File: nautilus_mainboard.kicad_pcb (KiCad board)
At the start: 4 copper layers, 176.2 x 77.5 mm, 52 parts, among them J18 179-UJ20CHC4SMTTR, J3 1761681-3, J4 Header male 1x05, J7 LPHT-04-16-L-RT1-GP, SW1 Button Switch SPST-No

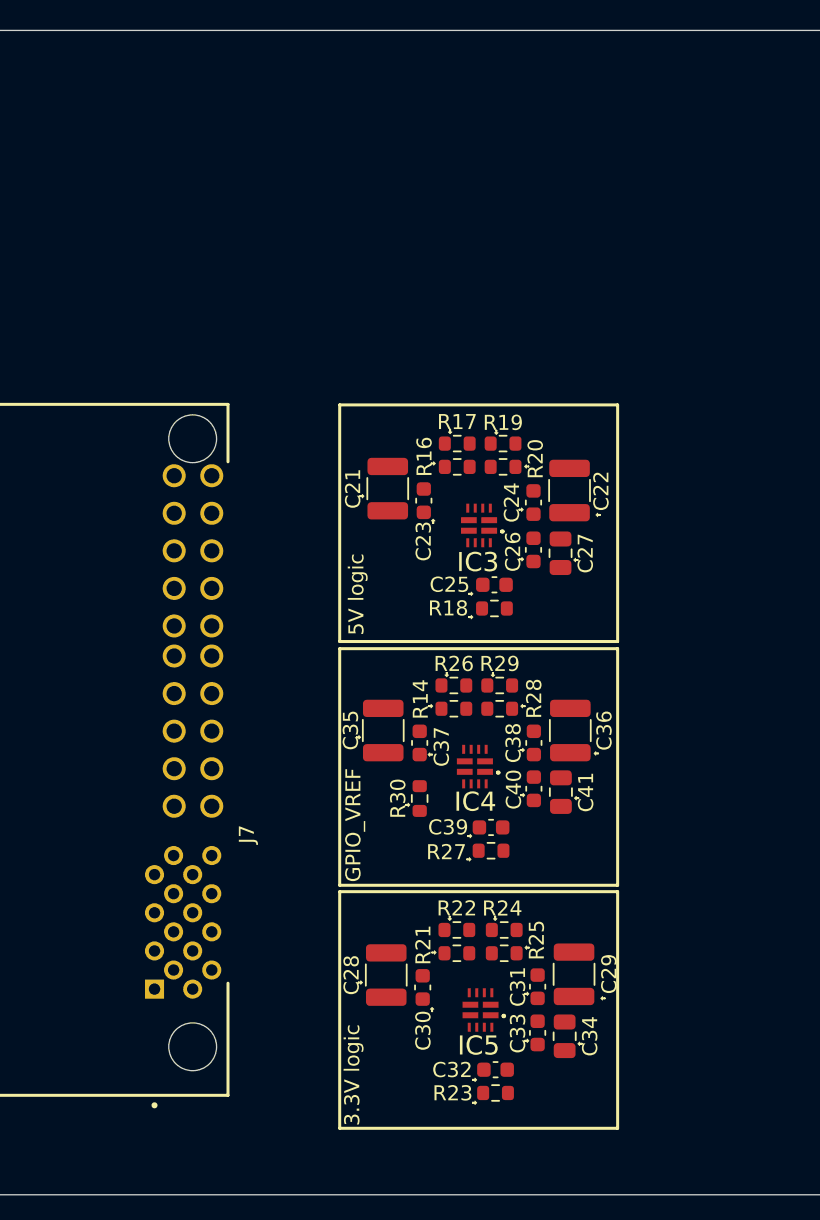
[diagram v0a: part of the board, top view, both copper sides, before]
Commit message: multiple changes to the differential pair for easier routing later.
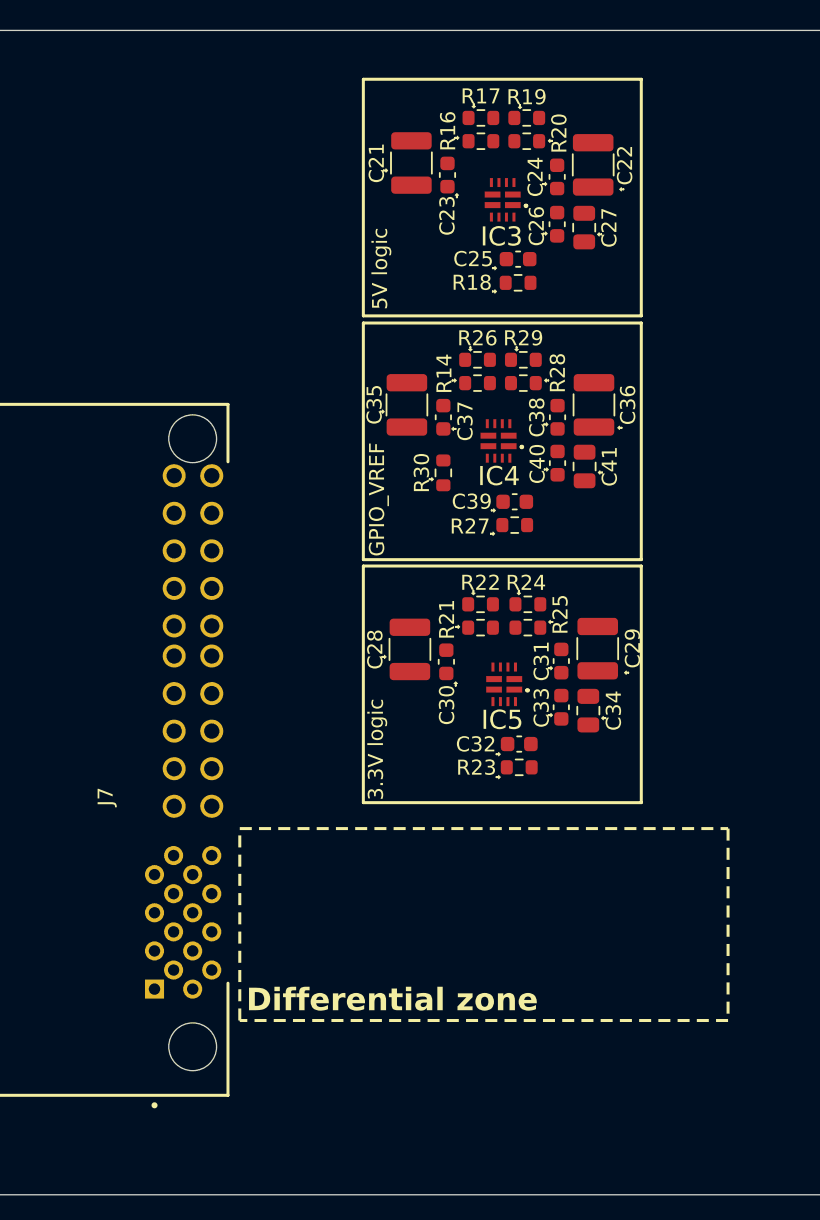
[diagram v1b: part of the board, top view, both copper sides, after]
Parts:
- moved C31 21.7 mm to (108.8, 89.5)
- moved R14 21.7 mm to (103.2, 71.0)
- moved R28 21.7 mm to (106.3, 71.0)
- moved C25 21.7 mm to (106.0, 62.7)
- moved C26 21.7 mm to (108.5, 60.4)
- moved IC3 21.7 mm to (104.9, 58.8)
- moved C21 21.7 mm to (98.8, 56.3)
- moved C22 21.7 mm to (111.0, 56.5)
- moved C23 21.7 mm to (101.2, 57.1)
- moved C24 21.7 mm to (108.5, 57.2)
- moved C27 21.7 mm to (110.3, 60.6)
- moved C28 21.7 mm to (98.8, 88.7)
- moved C29 21.7 mm to (111.2, 88.7)
- moved C30 21.7 mm to (101.2, 89.5)
- moved C32 21.7 mm to (106.0, 95.0)
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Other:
- board text added: "Differential zone"

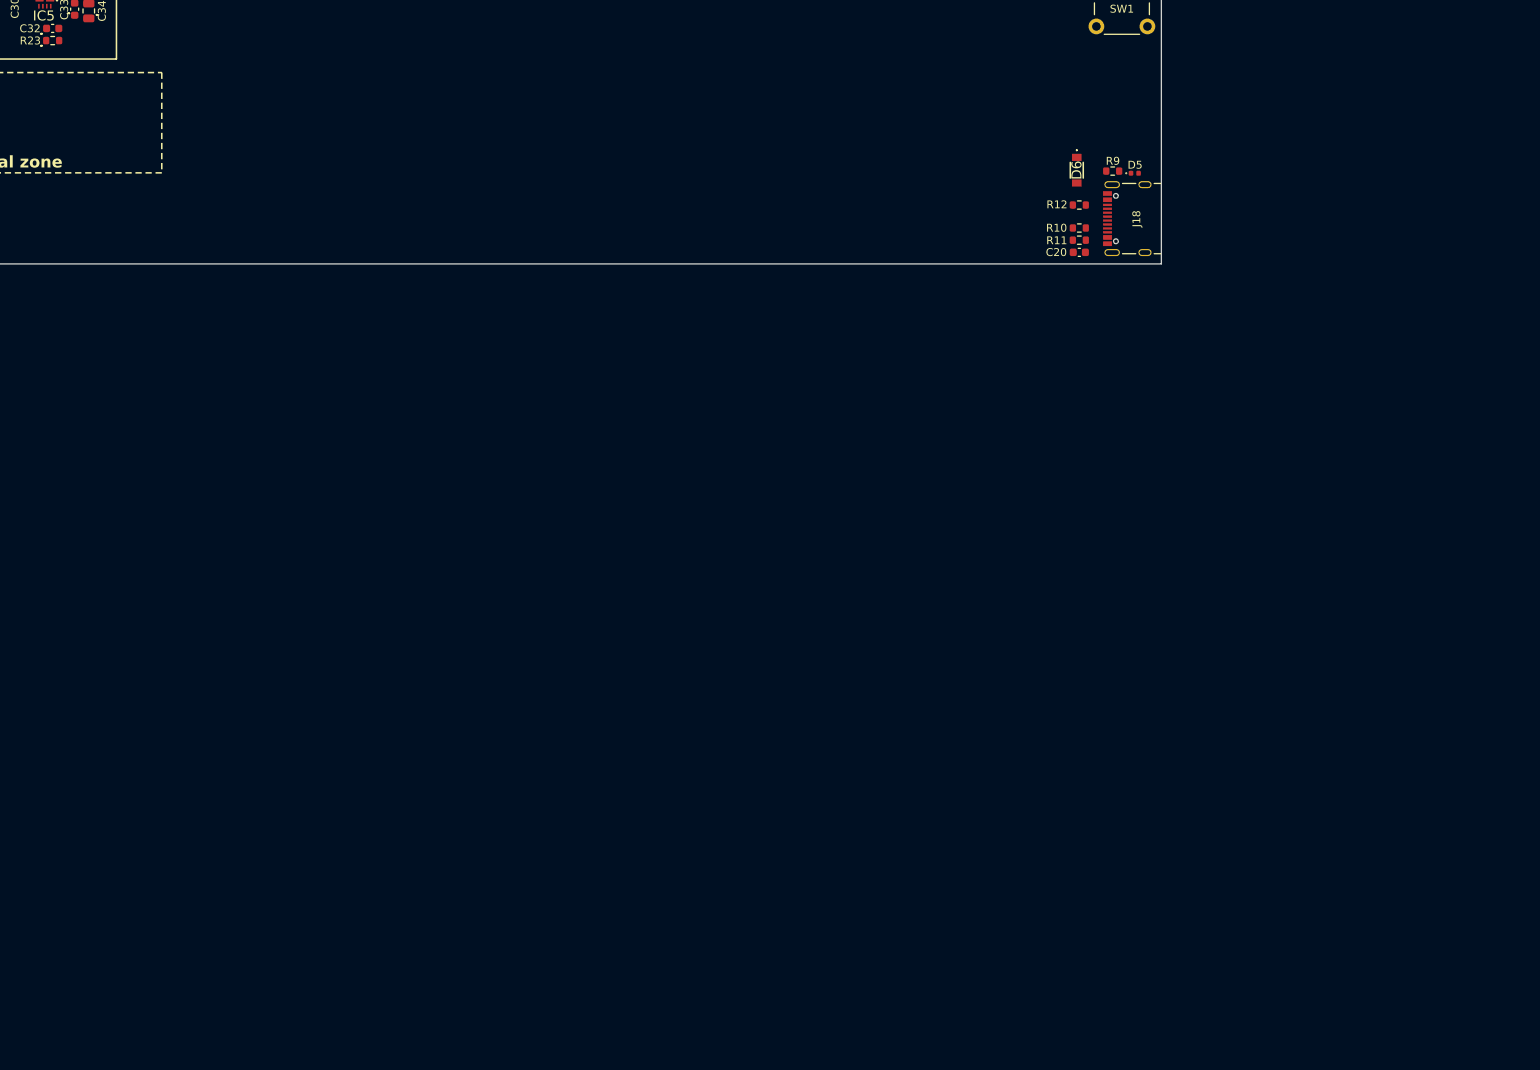
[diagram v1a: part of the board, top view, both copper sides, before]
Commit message: added Gyroscope and Accelerometer part (4x) over IIC
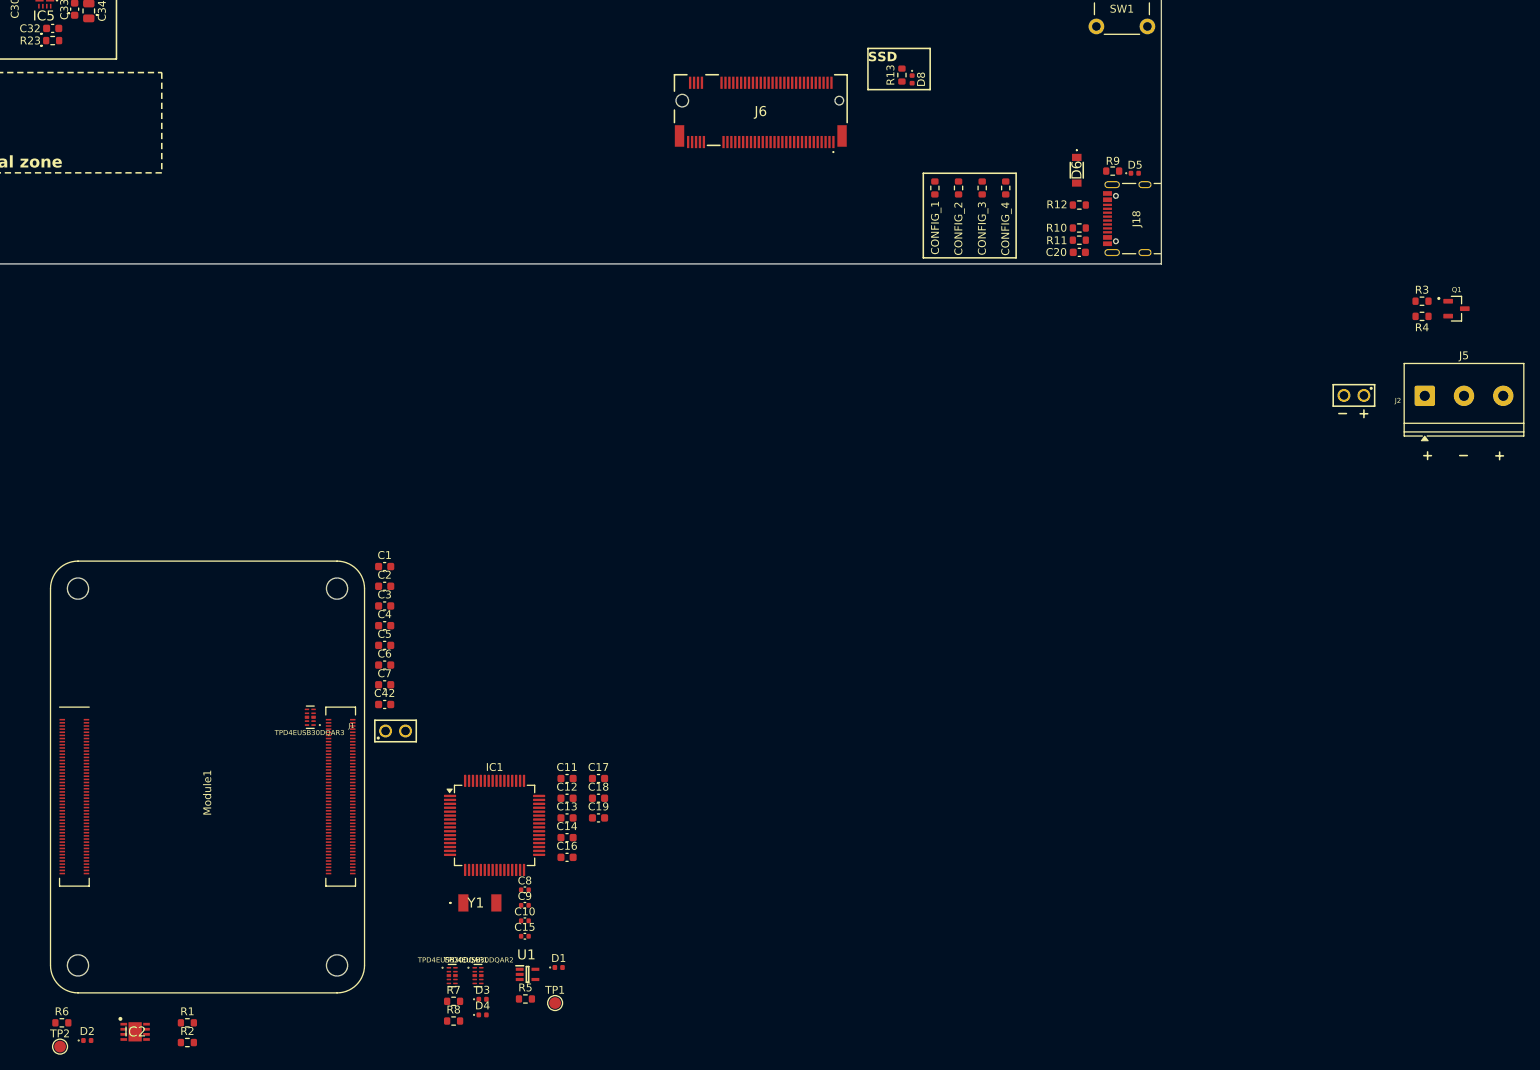
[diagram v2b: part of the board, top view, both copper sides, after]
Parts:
- added C1: 100nF, Capacitor_SMD:C_0603_1608Metric, F.Cu at (148.3, 163.6)
- added C10: 2.2pF, Capacitor_SMD:C_0402_1005Metric, F.Cu at (166.2, 208.7)
- added C11: 100nF, Capacitor_SMD:C_0603_1608Metric, F.Cu at (171.5, 190.6)
- added C12: 10pF, Capacitor_SMD:C_0603_1608Metric, F.Cu at (171.5, 193.1)
- added C13: 10pF, Capacitor_SMD:C_0603_1608Metric, F.Cu at (171.5, 195.6)
- added C14: 10pF, Capacitor_SMD:C_0603_1608Metric, F.Cu at (171.5, 198.1)
- added C15: 2.2pF, Capacitor_SMD:C_0402_1005Metric, F.Cu at (166.2, 210.6)
- added C16: 10pF, Capacitor_SMD:C_0603_1608Metric, F.Cu at (171.5, 200.6)
- added C17: 10pF, Capacitor_SMD:C_0603_1608Metric, F.Cu at (175.6, 190.6)
- added C18: 10pF, Capacitor_SMD:C_0603_1608Metric, F.Cu at (175.6, 193.1)
- added C19: 100nF, Capacitor_SMD:C_0603_1608Metric, F.Cu at (175.6, 195.6)
- added C2: 100nF, Capacitor_SMD:C_0603_1608Metric, F.Cu at (148.3, 166.1)
- added C3: 100nF, Capacitor_SMD:C_0603_1608Metric, F.Cu at (148.3, 168.6)
- added C4: 100nF, Capacitor_SMD:C_0603_1608Metric, F.Cu at (148.3, 171.1)
- added C42: 1uF, Capacitor_SMD:C_0603_1608Metric, F.Cu at (148.3, 181.1)
- added C5: 100nF, Capacitor_SMD:C_0603_1608Metric, F.Cu at (148.3, 173.6)
- added C6: 100nF, Capacitor_SMD:C_0603_1608Metric, F.Cu at (148.3, 176.1)
- added C7: 1uF, Capacitor_SMD:C_0603_1608Metric, F.Cu at (148.3, 178.6)
- added C8: 4.7pF, Capacitor_SMD:C_0402_1005Metric, F.Cu at (166.2, 204.7)
- added C9: 4.7pF, Capacitor_SMD:C_0402_1005Metric, F.Cu at (166.2, 206.7)
- added CONFIG_1: 0, Resistor_SMD:R_0603_1608Metric, F.Cu at (218.4, 115.3)
- added CONFIG_2: 0, Resistor_SMD:R_0603_1608Metric, F.Cu at (221.4, 115.3)
- added CONFIG_3: 0, Resistor_SMD:R_0603_1608Metric, F.Cu at (224.4, 115.3)
- added CONFIG_4: 0, Resistor_SMD:R_0603_1608Metric, F.Cu at (227.4, 115.3)
- added D1: APHHS1005LSECK/J3-PF, LED_SMD:LED_0402_1005Metric, F.Cu at (170.5, 214.6)
- added D2: APHHS1005LZGCK-V, LED_SMD:LED_0402_1005Metric, F.Cu at (110.4, 223.9)
- added D3: APHHS1005LSYCK/J3-PF, LED_SMD:LED_0402_1005Metric, F.Cu at (160.8, 218.7)
- added D4: APHHS1005LZGCK-V, LED_SMD:LED_0402_1005Metric, F.Cu at (160.8, 220.7)
- added D8: APHHS1005LCGCK, LED_SMD:LED_0402_1005Metric, F.Cu at (215.5, 101.5)
- added IC1: STM32H7B0RBT6, Package_QFP:LQFP-64_10x10mm_P0.5mm, F.Cu at (162.3, 196.5)
- added IC2: TCAN3414DRBR, dz_comm:TCAN3414DRBR, F.Cu at (116.5, 222.8)
- added J1: 61300211121, dz_con:Wurth_Con_61300211121, F.Cu at (149.7, 184.5)
- added J2: 61300211121, dz_con:Wurth_Con_61300211121, F.Cu at (271.8, 141.8)
- added J5: 1792876, TerminalBlock_Phoenix:TerminalBlock_Phoenix_PT-1,5-3-5.0-H_1x03_P5.00mm_Horizontal, F.Cu at (280.8, 141.8)
- added J6: MDT275M02001, dz_con:PCIE_MDT275M02001, F.Cu at (196.2, 105.4)
- added Module1: DF40C-100DS-0.4V(51), dz_con:Con-Raspberry-Pi-4-Compute-Module, F.Cu at (109.2, 214.4)
- added Q1: 50V, dz_dio:onsemi_Mosfet_BSS138, F.Cu at (284.8, 130.7)
- added R1: 2.2k, Resistor_SMD:R_0603_1608Metric, F.Cu at (123.2, 221.7)
- added R13: 1k, Resistor_SMD:R_0603_1608Metric, F.Cu at (214.2, 100.9)
- added R2: 4.3k, Resistor_SMD:R_0603_1608Metric, F.Cu at (123.2, 224.2)
- added R3: 1k, Resistor_SMD:R_0603_1608Metric, F.Cu at (280.4, 129.8)
- added R4: 0, Resistor_SMD:R_0603_1608Metric, F.Cu at (280.5, 131.7)
- added R5: 1k, Resistor_SMD:R_0603_1608Metric, F.Cu at (166.2, 218.6)
- added R6: 1k, Resistor_SMD:R_0603_1608Metric, F.Cu at (107.2, 221.7)
- added R7: 1k, Resistor_SMD:R_0603_1608Metric, F.Cu at (157.1, 218.9)
- added R8: 1k, Resistor_SMD:R_0603_1608Metric, F.Cu at (157.1, 221.4)
- added TP1: Test Point, TestPoint:TestPoint_Pad_D1.5mm, F.Cu at (170.0, 219.2)
- added TP2: Test Point, TestPoint:TestPoint_Pad_D1.5mm, F.Cu at (107.0, 224.7)
- added TPD4EUSB30DQAR1: ~, dz_con:IC_TPD4EUSB30DQAR, F.Cu at (156.9, 215.7)
- added TPD4EUSB30DQAR2: ~, dz_con:IC_TPD4EUSB30DQAR, F.Cu at (160.2, 215.7)
- added TPD4EUSB30DQAR3: ~, dz_con:IC_TPD4EUSB30DQAR, F.Cu at (138.8, 182.7)
- added U1: Buffers & Line Driver, dz_dio:SOT65P210X110-5N, F.Cu at (166.5, 215.5)
- added Y1: CC4V-T1A-32.768kHz-6pF-20PPM-TA-QC, dz_sens:CC4VT1A, F.Cu at (160.4, 206.4)
- IC3, IC4, IC5: value ~ -> TPS2121RUXT
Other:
- board text added: "SSD"
